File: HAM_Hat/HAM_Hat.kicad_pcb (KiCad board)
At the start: 2 copper layers, 65 x 56 mm, 45 parts, among them J101 TL212V-02P-G12S, J102 DB-9RS-C, J103 NCW254-02S, J104 SMA6252A2, J105 Conn_01x01, J106 Conn_01x01, J107 Conn_01x01, J108 Conn_01x01, J3 FHDH2.54-40, M101 Fan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

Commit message: Bump version: 1.0.0 → 1.0.1
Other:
- board text added: "v1.0.1"
- board text removed: "v1.0.0"
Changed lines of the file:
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@@
     (title "Ham hat")
     (date 2021-12-03)
-    (rev v1.0.0)
+    (rev v1.0.1)
     (company "Logonex Bt.")
     (comment 1 "Drawn by HA5OGL")
@@
     (effects (font (size 1.5 1.5) (thickness 0.3)))
   )
-  (gr_text v1.0.0 (at 110.6 103.7) (layer F.SilkS)
+  (gr_text v1.0.1 (at 110.6 103.7) (layer F.SilkS)
     (effects (font (size 1.5 1.5) (thickness 0.3)))
   )

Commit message: Fix outline
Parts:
- moved J101 38.7 mm to (157.8, 120.4)
- moved H4 38.6 mm to (177.5, 122.5)
- moved H1 38.6 mm to (119.5, 73.5)
- moved H3 38.6 mm to (119.5, 122.5)
- moved H2 38.6 mm to (177.5, 73.5)
- moved C101 38.6 mm to (175.6, 92.5)
- moved C103 38.6 mm to (165.1, 112.2)
- moved D102 38.6 mm to (175.7, 104.7)
- moved L101 38.6 mm to (166.7, 97.0)
- moved R101 38.6 mm to (165.6, 86.5)
- moved H101 38.6 mm to (122.5, 86.9)
- moved H102 38.6 mm to (122.5, 91.1)
- moved J102 38.6 mm to (144.2, 117.9)
- moved J105 38.6 mm to (132.7, 89.7)
- moved J106 38.6 mm to (132.7, 86.9)
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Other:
- board size 65 x 56 mm -> 65 x 56.5 mm

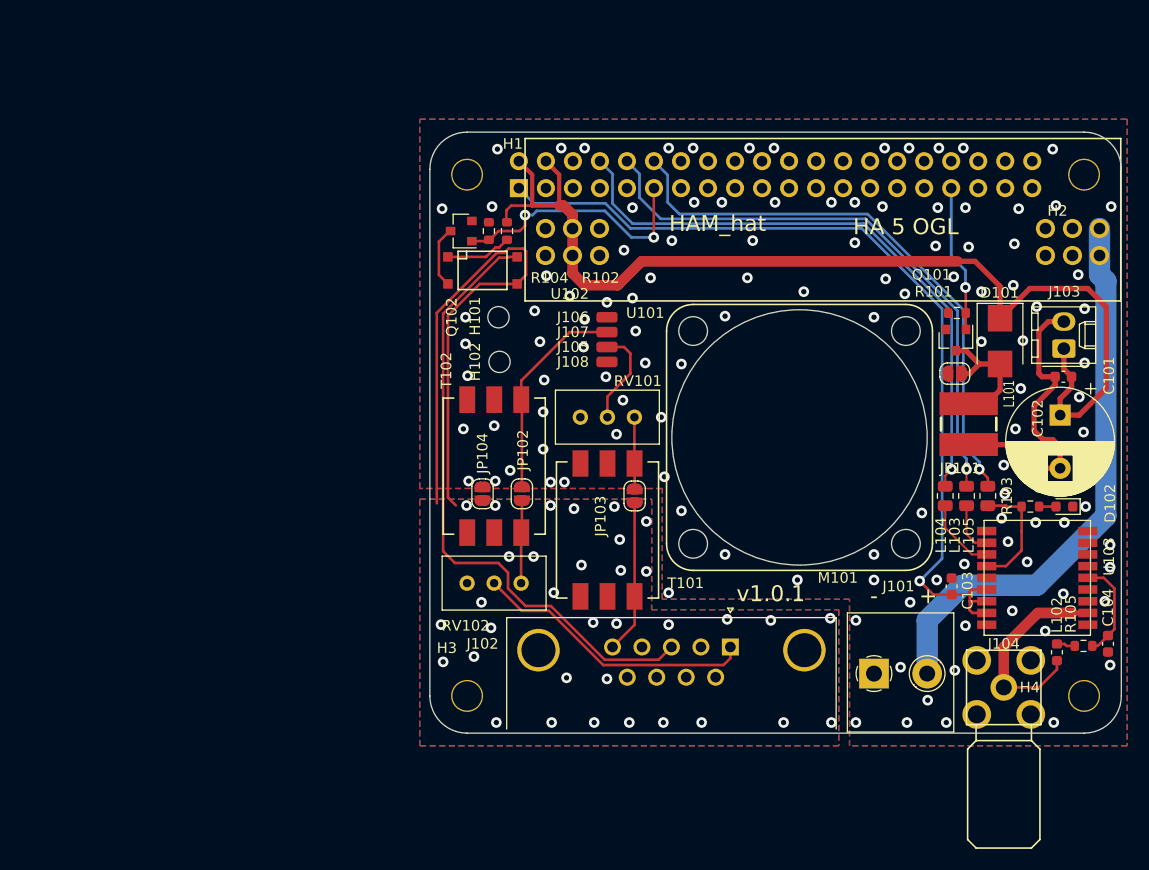
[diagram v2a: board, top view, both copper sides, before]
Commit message: Fix mechanical collisions with the PI
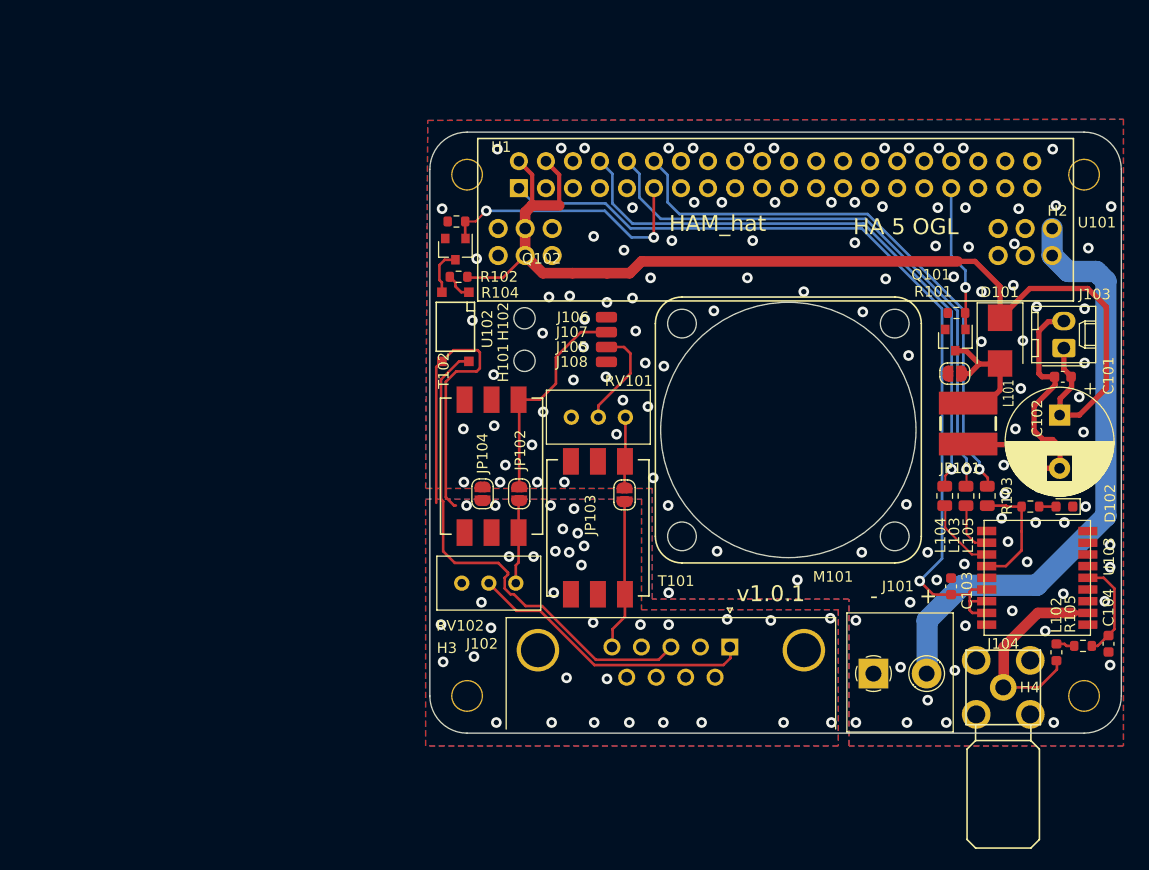
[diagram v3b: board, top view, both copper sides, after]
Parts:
- moved R104 6.26 mm to (118.7, 83.1), turned to 0 degrees
- moved U102 5.88 mm to (118.4, 87.8), turned to 270 degrees
- moved H101 4.78 mm to (124.9, 91.0)
- moved H102 4.73 mm to (124.9, 87.0)
- moved U101 4.45 mm to (174.5, 81.1)
- moved R102 3.18 mm to (118.5, 77.9), turned to 0 degrees
- moved Q102 1.79 mm to (118.4, 80.5), turned to 270 degrees
- moved M101 1.26 mm to (149.7, 97.5)
- moved JP103 0.96 mm to (134.3, 103.6)
- moved T101 0.92 mm to (131.8, 106.7)
- moved RV101 0.85 mm to (129.3, 96.3)
- moved RV102 0.50 mm to (119.0, 111.9)
- moved JP102 0.25 mm to (124.4, 103.5)
- moved T102 0.25 mm to (121.8, 100.9)
- moved L101 0.07 mm to (166.6, 96.9)
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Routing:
- net GNDA: track 58.2 -> 35.0 mm
- net Net-(J102-Pad3): track 58.5 -> 47.1 mm
- net /P5V_HAT: track 100.2 -> 104.8 mm
- net Net-(R104-Pad1): track 6.22 -> 2.61 mm
- net Net-(J101-Pad2): track 53.1 -> 56.5 mm
- net Net-(Q102-Pad3): track 5.84 -> 4.35 mm
- net /PTT: track 24.5 -> 25.4 mm
- net Net-(J107-Pad1): track 20.0 -> 20.6 mm
- net Net-(J102-Pad1): track 26.7 -> 27.4 mm
- net GND: vias 119 -> 118

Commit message: Bump version: 1.0.1 → 1.0.2
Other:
- board text added: "v1.0.2"
- board text removed: "v1.0.1"
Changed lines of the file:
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@@
     (title "Ham hat")
     (date 2021-12-03)
-    (rev v1.0.1)
+    (rev v1.0.2)
     (company "Logonex Bt.")
     (comment 1 "Drawn by HA5OGL")
@@
     (effects (font (size 1.5 1.5) (thickness 0.3)))
   )
-  (gr_text v1.0.1 (at 148.05 112.9) (layer F.SilkS)
+  (gr_text v1.0.2 (at 148.05 112.9) (layer F.SilkS)
     (effects (font (size 1.5 1.5) (thickness 0.3)))
   )

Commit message: Some optiomization
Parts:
- moved RV101 10.5 mm to (118.8, 96.3)
- moved T101 10.4 mm to (121.4, 106.8)
- moved JP103 10.3 mm to (124.0, 103.9)
- moved RV102 10.2 mm to (129.2, 111.7)
- moved T102 10.0 mm to (131.8, 101.2)
- moved JP102 9.90 mm to (134.3, 103.4)
- moved C101 0.90 mm to (174.6, 92.5)
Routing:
- net Net-(J102-Pad1): track 27.4 -> 17.2 mm
- net Net-(J102-Pad5): track 14.2 -> 20.0 mm
- net Net-(J105-Pad1): track 9.70 -> 14.8 mm
- net Net-(J107-Pad1): track 20.6 -> 16.5 mm
- net Net-(J102-Pad3): track 47.1 -> 49.2 mm
- net Net-(C101-Pad2): track 28.8 -> 27.4 mm
- net /P5V_HAT: track 104.8 -> 104.1 mm
- net GNDA: vias 34 -> 35
- net GND: vias 118 -> 117

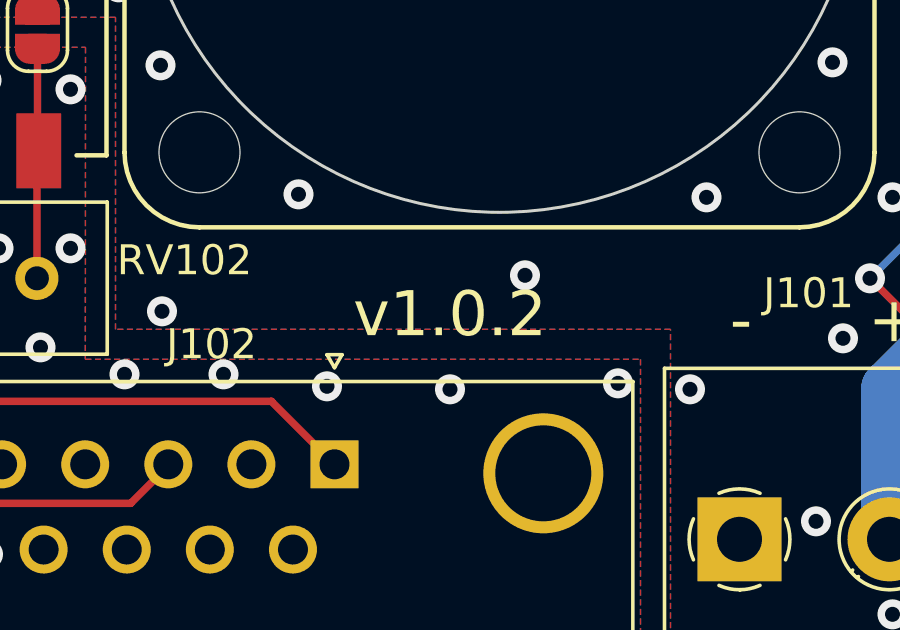
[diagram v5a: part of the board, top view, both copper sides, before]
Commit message: Bump version: 1.0.2 → 1.0.3
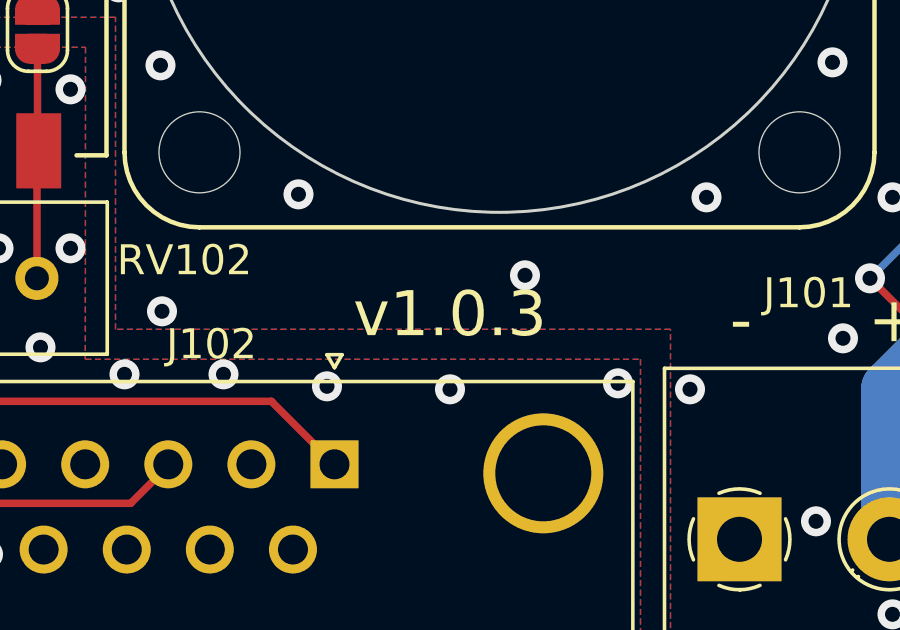
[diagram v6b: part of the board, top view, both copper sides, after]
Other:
- board text added: "v1.0.3"
- board text removed: "v1.0.2"
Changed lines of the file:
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@@
     (title "Ham hat")
     (date 2021-12-03)
-    (rev v1.0.2)
+    (rev v1.0.3)
     (company "Logonex Bt.")
     (comment 1 "Drawn by HA5OGL")
@@
     (effects (font (size 1.5 1.5) (thickness 0.3)))
   )
-  (gr_text v1.0.2 (at 148.05 112.9) (layer F.SilkS)
+  (gr_text v1.0.3 (at 148.05 112.9) (layer F.SilkS)
     (effects (font (size 1.5 1.5) (thickness 0.3)))
   )

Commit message: More fixes
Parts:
- moved JP103 0.40 mm to (124.0, 103.5)
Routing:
- net Net-(J102-Pad1): track 17.2 -> 16.2 mm
- net GNDA: vias 35 -> 36
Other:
- net class Default: trace_width 0.2 -> 0.25
- rule trace_min: 0.15 -> 0.25

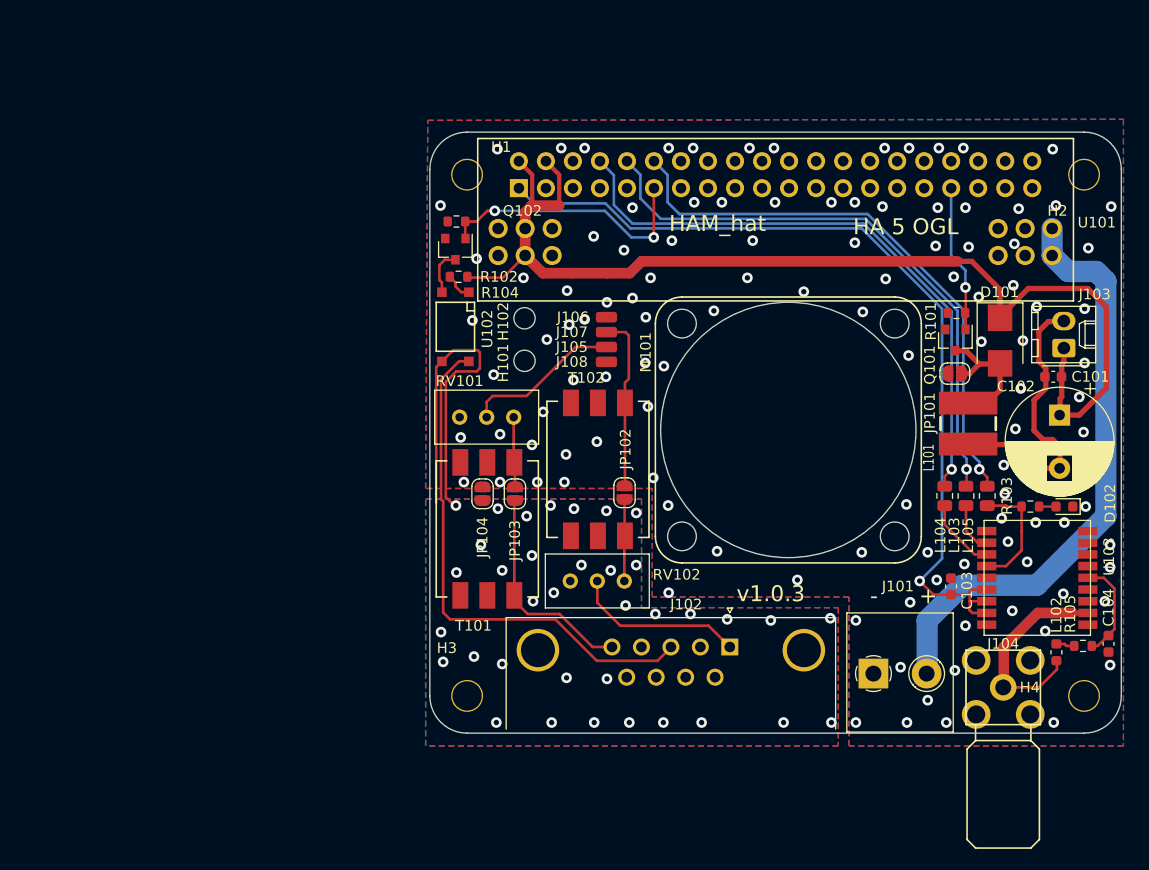
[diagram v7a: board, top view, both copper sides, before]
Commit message: Add RTC
Also add header socket for audio connection.
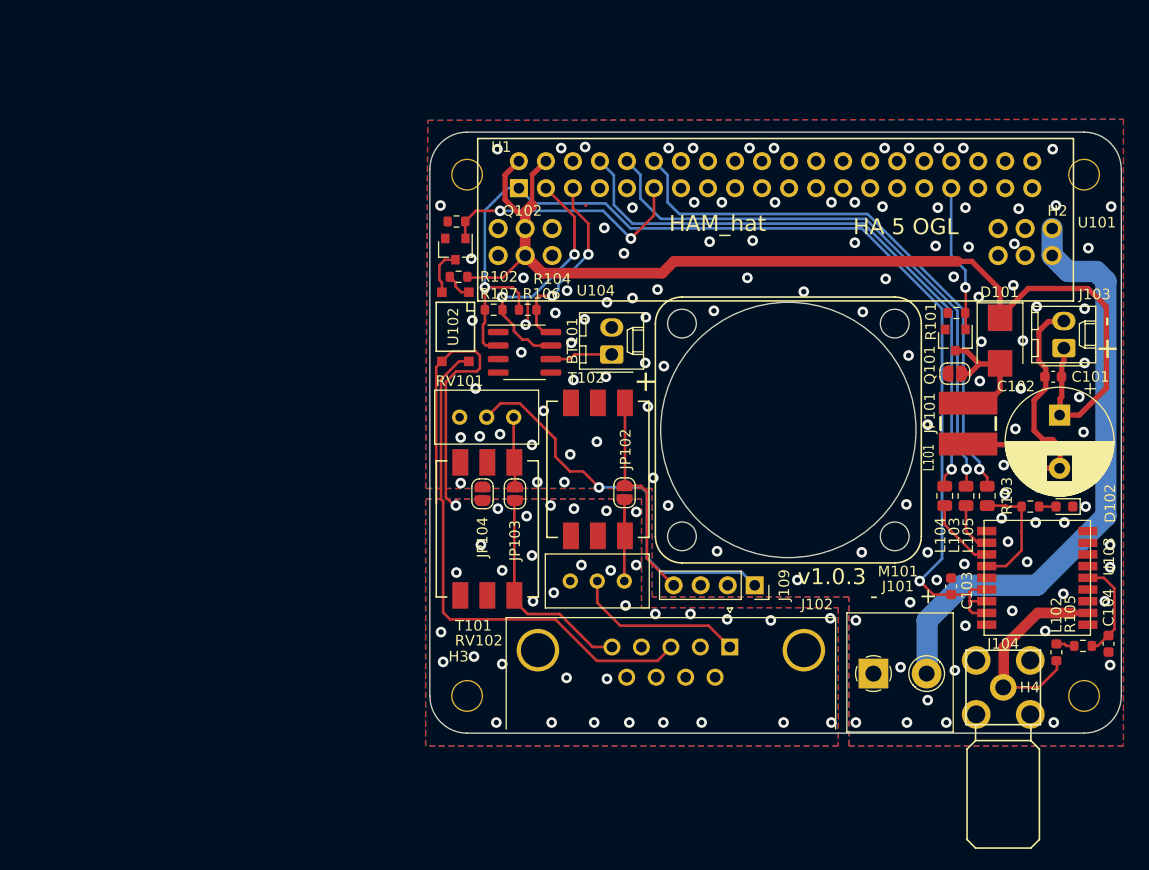
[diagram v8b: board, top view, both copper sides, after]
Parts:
- removed H101, H102: 2mm_Mounting_Hole, MountingHole:MountingHole_2mm
- removed J105, J106, J107, J108: Conn_01x01, Connector_Wire:SolderWirePad_1x01_SMD_1x2mm
- added BT101: Battery_Cell, Connector_Molex:Molex_KK-254_AE-6410-02A_1x02_P2.54mm_Vertical, F.Cu at (133.1, 90.4)
- added J109: Conn_01x05, Connector_PinSocket_2.54mm:PinSocket_1x04_P2.54mm_Vertical, F.Cu at (146.5, 112.1)
- added R106: 10k, Resistor_SMD:R_0603_1608Metric, F.Cu at (125.2, 86.2)
- added R107: 10k, Resistor_SMD:R_0603_1608Metric, F.Cu at (122.0, 86.2)
- added U104: DS3231MZ, Package_SO:SOIC-8_3.9x4.9mm_P1.27mm, F.Cu at (124.9, 90.2)
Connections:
- J3 pad 3: (no net) -> /SDA
- J3 pad 5: (no net) -> /SCL
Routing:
- net /SDA: track 0.00 -> 23.5 mm, vias 0 -> 2
- net /P3V3_HAT: track 82.9 -> 106.0 mm, vias 1 -> 2
- net Net-(J109-Pad1): track 14.8 -> 37.4 mm, vias 0 -> 1
- net /SCL: track 0.00 -> 17.9 mm, vias 0 -> 2
- net Net-(BT101-Pad1): track 0.00 -> 5.91 mm
- net Net-(J109-Pad4): track 16.5 -> 20.0 mm
- net GND: track 0.00 -> 2.43 mm, vias 117 -> 120
- net /PTT: track 25.4 -> 24.3 mm
- net /P5V_HAT: track 104.1 -> 103.5 mm
